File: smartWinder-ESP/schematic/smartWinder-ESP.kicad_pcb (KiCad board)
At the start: 2 copper layers, 36.2 x 27.9 mm, 39 parts, among them IC2 MP2315GJ-Z, J1 Conn_01x09, J2 Conn_01x06, U1 LTV-847S, U2 ESP-12E

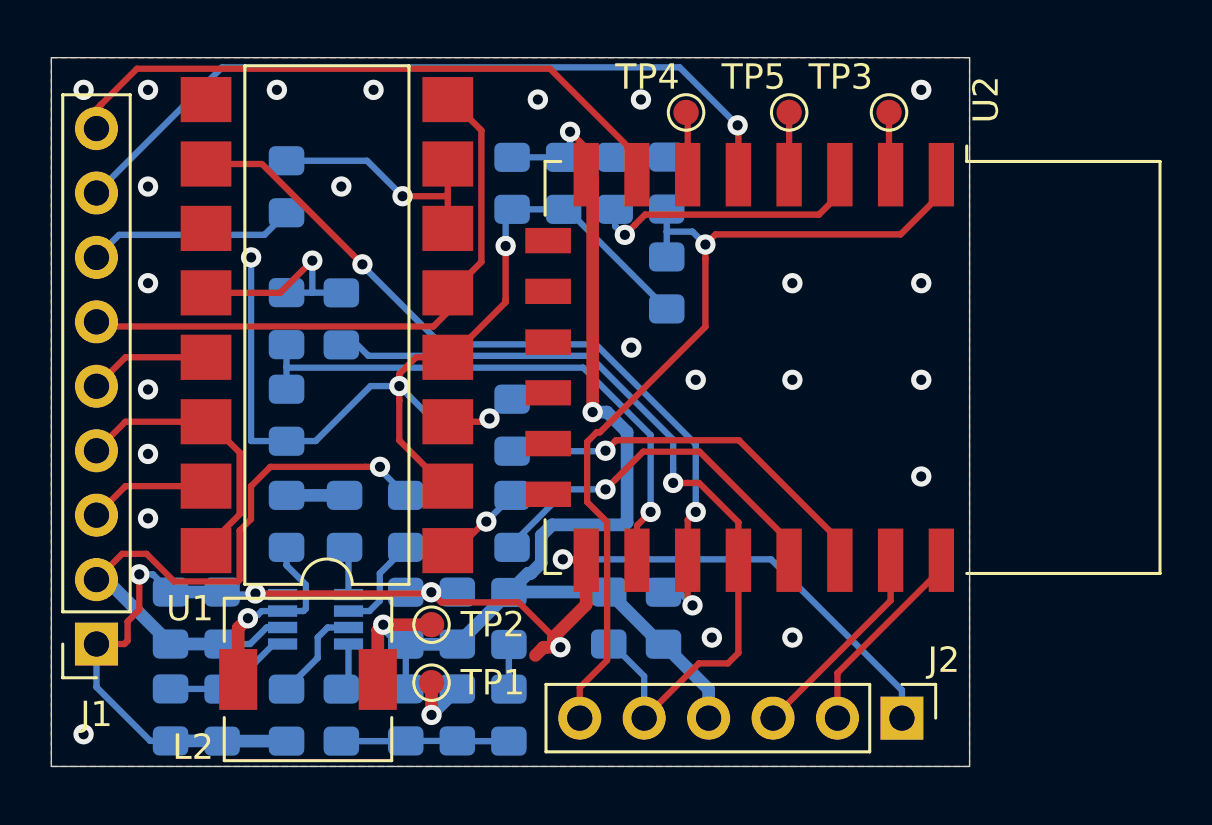
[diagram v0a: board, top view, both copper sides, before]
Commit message: Added VIN Sensing to the PCB
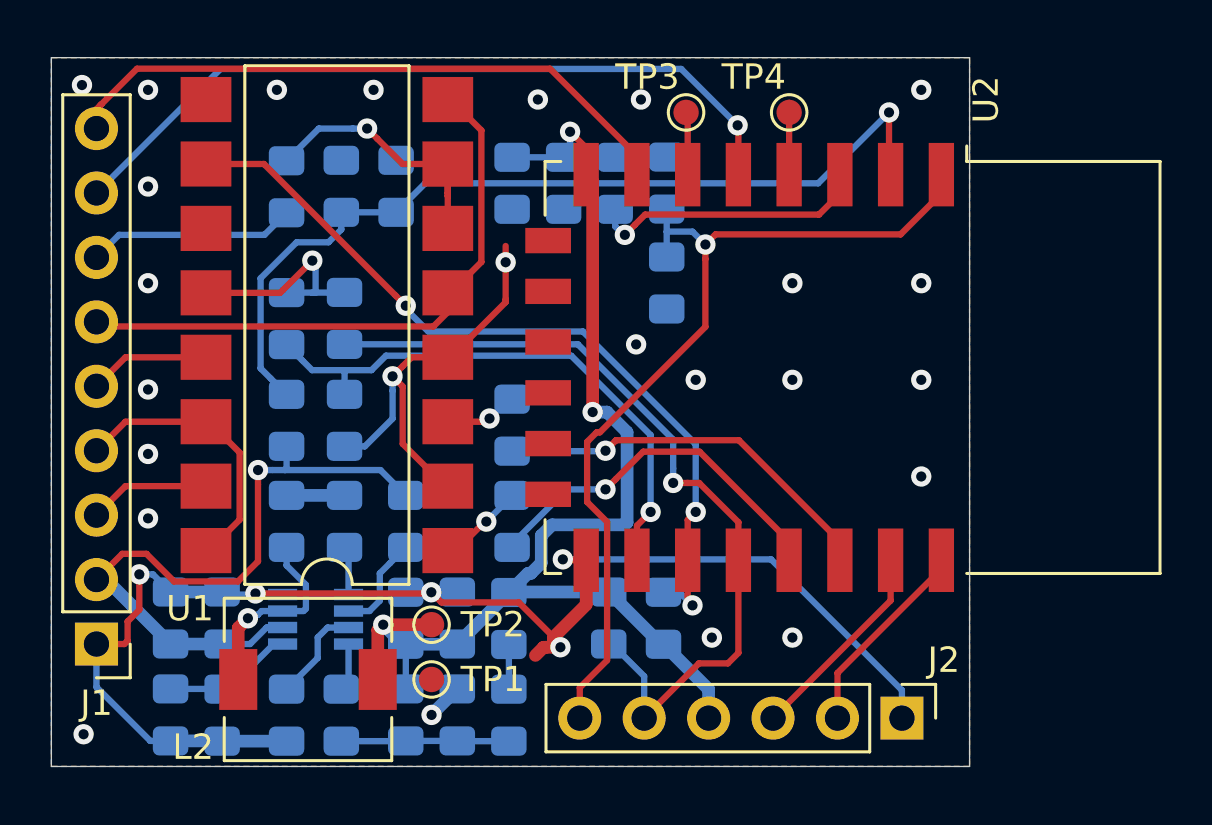
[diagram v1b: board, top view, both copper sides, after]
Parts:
- removed the TP3 at (105.4, 61.8)
- added C12: 100nF, Capacitor_SMD:C_0805_2012Metric_Pad1.15x1.40mm_HandSolder, B.Cu at (86.0, 64.8)
- added R18: 430k, Resistor_SMD:R_0805_2012Metric_Pad1.15x1.40mm_HandSolder, B.Cu at (81.7, 74.0)
- added R19: 10k, Resistor_SMD:R_0805_2012Metric_Pad1.15x1.40mm_HandSolder, B.Cu at (83.8, 64.8)
- J1: footprint Connector_PinSocket_2.54mm:PinSocket_1x09_P2.54mm_Vertical -> Connector_PinHeader_2.54mm:PinHeader_1x09_P2.54mm_Vertical
- moved R17 2.29 mm to (83.9, 74.0)
- moved R11 0.13 mm to (83.9, 70.0)
- moved TP1 0.13 mm to (87.4, 84.2)
- renumbered TP4 to TP3, TP5 to TP4
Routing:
- net Net-(C12-Pad1): track 2.99 -> 35.9 mm, vias 0 -> 1
- net GND: track 99.5 -> 78.4 mm, vias 32 -> 29
- net Net-(R10-Pad1): track 9.48 -> 11.3 mm
- net +24V: track 26.0 -> 27.0 mm
- net Net-(R18-Pad2): vias 0 -> 1

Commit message: Finalized PCB and sent to Production
Finalized PCB and sent to Production
Generated PDF and 3D PCB File
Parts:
- R10: value 10 k -> 10k
- R13, R14, R15, R16, R17: value 12k -> 10k
- renumbered TP2 to 3V3, TP1 to GND, TP3 to IO12, TP4 to IO16
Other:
- board text added: "smartWinder-ESP v1.0"
